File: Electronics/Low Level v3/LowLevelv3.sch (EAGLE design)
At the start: 66 parts, among them IC2 MCP4802, K1 ORWH-SH-105D1F,000, K3 ORWH-SH-105D1F,000, Q1 16MHz, T1 2N3904, T2 2N3904, U1 284512-4, U4 MCP2515, U5 MCP2551DIL08, X3 Motor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

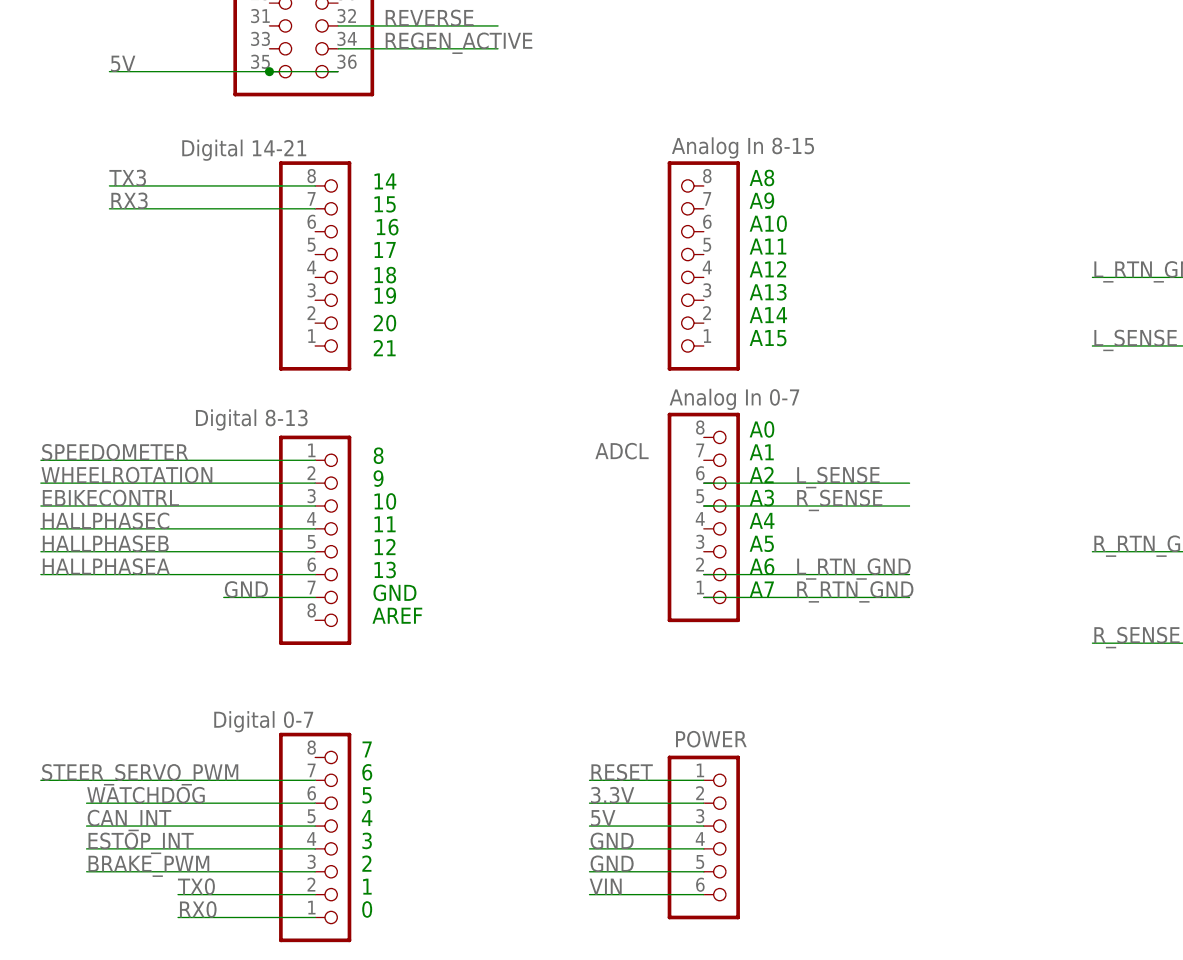
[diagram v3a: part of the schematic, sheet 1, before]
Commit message: corrected PCINT pin mapping
moved pretty much every interrupt pin to A8-A15, which had the secondary benefit of greatly reducing their trace length.
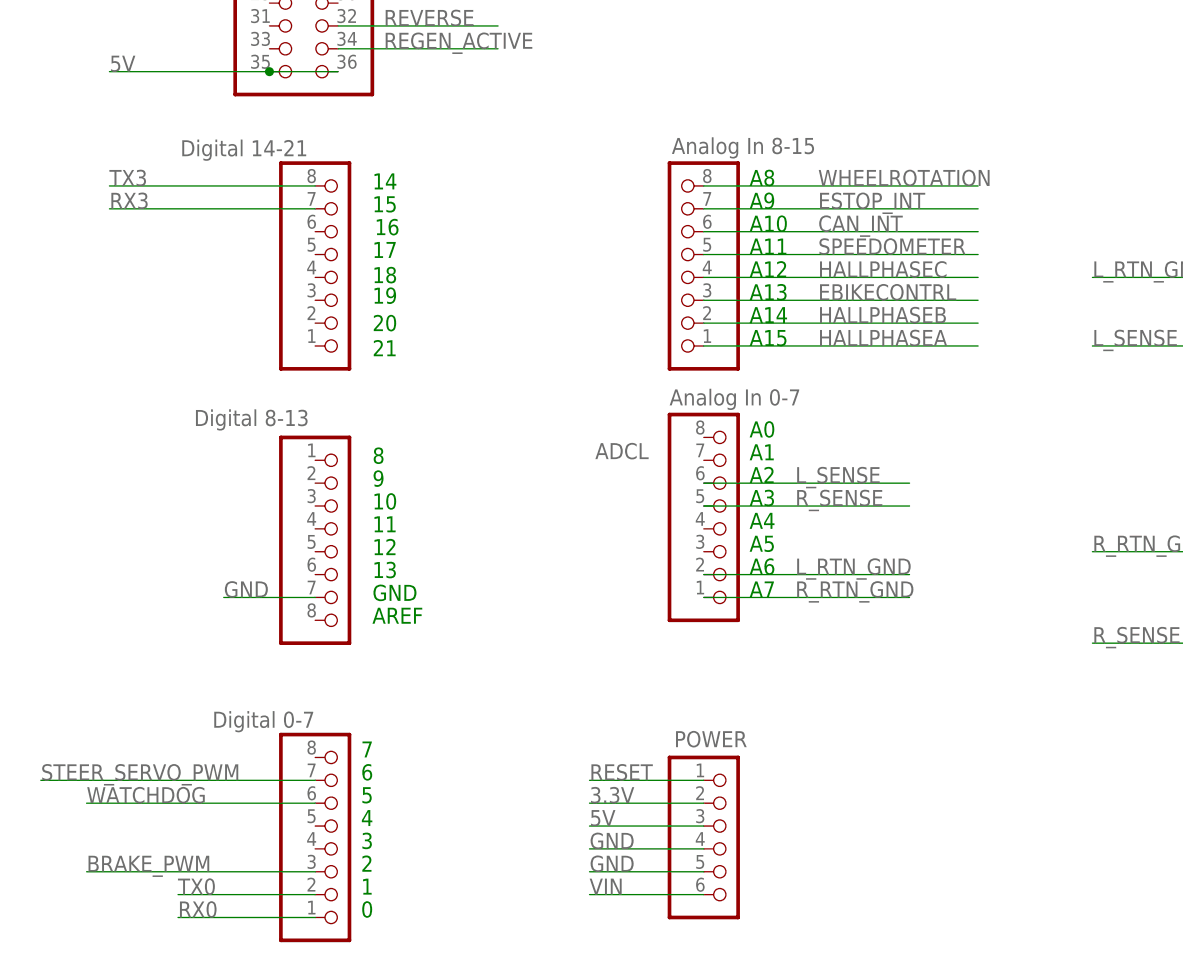
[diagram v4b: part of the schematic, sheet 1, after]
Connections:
- net CAN_INT: now also ADCH.6; no longer DIGITAL_0-7.5
- net EBIKECONTRL: now also ADCH.3; no longer DIGITAL_8-13.3
- net ESTOP_INT: now also ADCH.7; no longer DIGITAL_0-7.4
- net HALLPHASEA: now also ADCH.1; no longer DIGITAL_8-13.6
- net HALLPHASEB: now also ADCH.2; no longer DIGITAL_8-13.5
- net HALLPHASEC: now also ADCH.4; no longer DIGITAL_8-13.4
- net SPEEDOMETER: now also ADCH.5; no longer DIGITAL_8-13.1
- net WHEELROTATION: now also ADCH.8; no longer DIGITAL_8-13.2
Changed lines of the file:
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@@
 </segment>
 <segment>
-<label x="22.86" y="66.04" size="1.778" layer="95"/>
-<pinref part="DIGITAL_8-13" gate="A" pin="1"/>
-<wire x1="53.34" y1="66.04" x2="22.86" y2="66.04" width="0.1524" layer="91"/>
+<label x="109.22" y="88.9" size="1.778" layer="95"/>
+<pinref part="ADCH" gate="A" pin="5"/>
+<wire x1="127" y1="88.9" x2="96.52" y2="88.9" width="0.1524" layer="91"/>
 </segment>
 </net>
 <net name="HALLPHASEB" class="0">
 <segment>
-<label x="22.86" y="55.88" size="1.778" layer="95"/>
-<pinref part="DIGITAL_8-13" gate="A" pin="5"/>
-<wire x1="53.34" y1="55.88" x2="22.86" y2="55.88" width="0.1524" layer="91"/>
+<label x="109.22" y="81.28" size="1.778" layer="95"/>
+<pinref part="ADCH" gate="A" pin="2"/>
+<wire x1="96.52" y1="81.28" x2="127" y2="81.28" width="0.1524" layer="91"/>
 </segment>
 <segment>
@@
 <net name="WHEELROTATION" class="0">
 <segment>
-<label x="22.86" y="63.5" size="1.778" layer="95"/>
-<pinref part="DIGITAL_8-13" gate="A" pin="2"/>
-<wire x1="53.34" y1="63.5" x2="22.86" y2="63.5" width="0.1524" layer="91"/>
+<label x="109.22" y="96.52" size="1.778" layer="95"/>
+<pinref part="ADCH" gate="A" pin="8"/>
+<wire x1="96.52" y1="96.52" x2="127" y2="96.52" width="0.1524" layer="91"/>
 </segment>
 </net>
@@
 <net name="HALLPHASEA" class="0">
 <segment>
-<label x="22.86" y="53.34" size="1.778" layer="95"/>
-<pinref part="DIGITAL_8-13" gate="A" pin="6"/>
-<wire x1="53.34" y1="53.34" x2="22.86" y2="53.34" width="0.1524" layer="91"/>
+<label x="109.22" y="78.74" size="1.778" layer="95"/>
+<pinref part="ADCH" gate="A" pin="1"/>
+<wire x1="96.52" y1="78.74" x2="127" y2="78.74" width="0.1524" layer="91"/>
 </segment>
 <segment>
@@
 <net name="HALLPHASEC" class="0">
 <segment>
-<label x="22.86" y="58.42" size="1.778" layer="95"/>
-<pinref part="DIGITAL_8-13" gate="A" pin="4"/>
-<wire x1="53.34" y1="58.42" x2="22.86" y2="58.42" width="0.1524" layer="91"/>
+<label x="109.22" y="86.36" size="1.778" layer="95"/>
+<pinref part="ADCH" gate="A" pin="4"/>
+<wire x1="96.52" y1="86.36" x2="127" y2="86.36" width="0.1524" layer="91"/>
 </segment>
 <segment>
@@
 <net name="EBIKECONTRL" class="0">
 <segment>
-<label x="22.86" y="60.96" size="1.778" layer="95"/>
-<pinref part="DIGITAL_8-13" gate="A" pin="3"/>
-<wire x1="53.34" y1="60.96" x2="22.86" y2="60.96" width="0.1524" layer="91"/>
+<label x="109.22" y="83.82" size="1.778" layer="95"/>
+<pinref part="ADCH" gate="A" pin="3"/>
+<wire x1="96.52" y1="83.82" x2="127" y2="83.82" width="0.1524" layer="91"/>
 </segment>
 <segment>
@@
 <net name="CAN_INT" class="0">
 <segment>
-<label x="27.94" y="25.4" size="1.778" layer="95"/>
-<pinref part="DIGITAL_0-7" gate="A" pin="5"/>
-<wire x1="53.34" y1="25.4" x2="27.94" y2="25.4" width="0.1524" layer="91"/>
+<label x="109.22" y="91.44" size="1.778" layer="95"/>
+<pinref part="ADCH" gate="A" pin="6"/>
+<wire x1="96.52" y1="91.44" x2="127" y2="91.44" width="0.1524" layer="91"/>
 </segment>
 </net>
@@
 <net name="ESTOP_INT" class="0">
 <segment>
-<pinref part="DIGITAL_0-7" gate="A" pin="4"/>
-<wire x1="53.34" y1="22.86" x2="27.94" y2="22.86" width="0.1524" layer="91"/>
-<label x="27.94" y="22.86" size="1.778" layer="95"/>
-</segment>
-<segment>
+<label x="109.22" y="93.98" size="1.778" layer="95"/>
+<pinref part="ADCH" gate="A" pin="7"/>
+<wire x1="96.52" y1="93.98" x2="127" y2="93.98" width="0.1524" layer="91"/>
+</segment>
+<segment>

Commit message: board cleanup, via removal, silkscreen tidying
* Changing size of almost every 'tvalue' item
* slightly tweaked trace location to allow for greater ground plane coverage
* removed redundant ground vias
* began renaming devices for clarity
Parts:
- C3, C5, C8, C9: value 1 uF -> 1uF
- R3, R4, R8, R9: value 4.7 K -> 4.7K
- renumbered IC2 to IC3_4802, K1 to PB2_12/24, K3 to PB1_BRAKE_ON, U1 to X1, U4 to IC1_2515, U5 to IC2_2551

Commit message: lots of renaming and slight position changes
* renamed caps and resistors to make populating the board a little easier
* moved silk around to try and be a little more coherent
* slight copper adjustments to get more ground fill
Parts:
- C1, C2: value 0.1uF -> 1uF
- C11: value 33pF -> 0.1uF
- C13: value 560pF -> 0.1uF
- C4: value 1 uF -> 1uF
- C5: value 1uF -> 33pF
- C8: value 1uF -> 560pF
- C9: value 1uF -> 1 uF
- R1, R2: value 1K -> 4.7K
- R10: value 100 -> 120
- R11: value 4.7K -> 10k
- R12: value 120 -> 10k
- R13, R18: value 10k -> 1K
- R14: value 1K -> 20K
- R15: value 20K -> 10k
- R17: value 10k -> 4.7K
- R19: value 4.7K -> 1K
- R8: value 4.7K -> 100
- renumbered D5 to D4
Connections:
- net 5V: now also C11.1, C13.1, R14.1, R17.1; no longer C1.1, C2.1, R15.1, R19.1
- net BRAKE_ON: now also R18.1; no longer R6.1
- net CANH: now also R10.2; no longer R12.2
- net CANL: now also R10.1, R8.2; no longer R10.2, R12.1
- net ESTOP_INT: now also R15.1; no longer R17.1
- net GND: now also R12.2, R9.2; no longer R11.2, R18.2
- net L_RET: now also R2.2; no longer R9.2
- net L_RTN_GND: now also C2.1, R2.1; no longer C5.1, R9.1
- net L_SENSE: now also C1.1, R1.1; no longer C8.1, R4.1
- net L_STR: now also R1.2; no longer R4.2
- net N$1: now also R11.2, R12.1; no longer R13.2, R16.1
- net N$10: now also C8.1; no longer C13.1
- net N$12: now also R19.1; no longer R1.1
- net N$13: now also R19.2; no longer R1.2
- net N$14: now also R9.1; no longer R11.1
- net N$3: now also R6.1; no longer R2.1
- net N$4: now also R13.2; no longer R15.2
- net N$6: now also R6.2; no longer R2.2
- net N$7: now also R18.2; no longer R6.2
- net N$8: now also R15.2, R16.1; no longer R17.2, R18.1
- net N$9: now also R8.1; no longer R10.1
- net OSC2: now also C5.1; no longer C11.1
- net RESET: now also R11.1; no longer R13.1
- net RS: now also R13.1; no longer R14.1
- net R_RET: now also R4.2; no longer R8.2
- net R_RTN_GND: now also C4.1, R4.1; no longer C9.1, R8.1
- net WHEELROTATION: now also C9.1, R17.2; no longer C4.1, R19.2
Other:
- moved on the sheet: C11, C13, R11, R13, R14, R15, R16, R17, R4, R6

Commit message: Checkpoint for first PCB order
* few minor routing changes
* extended a 1x8 to a 1x10 because some Mega boards have two more pins on one header.
* added partial bill of materials
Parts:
- DIGITAL_8-13: device pinhead:PINHD-1X8 -> pinhead:PINHD-1X10
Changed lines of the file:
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@@
 <grid distance="0.1" unitdist="inch" unit="inch" style="lines" multiple="1" display="no" altdistance="0.01" altunitdist="inch" altunit="inch"/>
 <layers>
-<layer number="1" name="Top" color="4" fill="1" visible="yes" active="no"/>
-<layer number="2" name="Route2" color="1" fill="3" visible="yes" active="no"/>
-<layer number="3" name="Route3" color="4" fill="3" visible="yes" active="no"/>
-<layer number="4" name="Route4" color="1" fill="4" visible="yes" active="no"/>
-<layer number="5" name="Route5" color="4" fill="4" visible="yes" active="no"/>
-<layer number="6" name="Route6" color="1" fill="8" visible="yes" active="no"/>
-<layer number="7" name="Route7" color="4" fill="8" visible="yes" active="no"/>
-<layer number="8" name="Route8" color="1" fill="2" visible="yes" active="no"/>
-<layer number="9" name="Route9" color="4" fill="2" visible="yes" active="no"/>
-<layer number="10" name="Route10" color="1" fill="7" visible="yes" active="no"/>
-<layer number="11" name="Route11" color="4" fill="7" visible="yes" active="no"/>
-<layer number="12" name="Route12" color="1" fill="5" visible="yes" active="no"/>
-<layer number="13" name="Route13" color="4" fill="5" visible="yes" active="no"/>
-<layer number="14" name="Route14" color="1" fill="6" visible="yes" active="no"/>
-<layer number="15" name="Route15" color="4" fill="6" visible="yes" active="no"/>
-<layer number="16" name="Bottom" color="1" fill="1" visible="yes" active="no"/>
-<layer number="17" name="Pads" color="2" fill="1" visible="yes" active="no"/>
-<layer number="18" name="Vias" color="2" fill="1" visible="yes" active="no"/>
-<layer number="19" name="Unrouted" color="6" fill="1" visible="yes" active="no"/>
-<layer number="20" name="Dimension" color="15" fill="1" visible="yes" active="no"/>
-<layer number="21" name="tPlace" color="7" fill="1" visible="yes" active="no"/>
-<layer number="22" name="bPlace" color="7" fill="1" visible="yes" active="no"/>
-<layer number="23" name="tOrigins" color="15" fill="1" visible="yes" active="no"/>
-<layer number="24" name="bOrigins" color="15" fill="1" visible="yes" active="no"/>
-<layer number="25" name="tNames" color="7" fill="1" visible="yes" active="no"/>
-<layer number="26" name="bNames" color="7" fill="1" visible="yes" active="no"/>
-<layer number="27" name="tValues" color="7" fill="1" visible="yes" active="no"/>
-<layer number="28" name="bValues" color="7" fill="1" visible="yes" active="no"/>
+<layer number="1" name="Top" color="4" fill="1" visible="no" active="no"/>
+<layer number="2" name="Route2" color="1" fill="3" visible="no" active="no"/>
+<layer number="3" name="Route3" color="4" fill="3" visible="no" active="no"/>
+<layer number="4" name="Route4" color="1" fill="4" visible="no" active="no"/>
+<layer number="5" name="Route5" color="4" fill="4" visible="no" active="no"/>
+<layer number="6" name="Route6" color="1" fill="8" visible="no" active="no"/>
+<layer number="7" name="Route7" color="4" fill="8" visible="no" active="no"/>
+<layer number="8" name="Route8" color="1" fill="2" visible="no" active="no"/>
+<layer number="9" name="Route9" color="4" fill="2" visible="no" active="no"/>
+<layer number="10" name="Route10" color="1" fill="7" visible="no" active="no"/>
+<layer number="11" name="Route11" color="4" fill="7" visible="no" active="no"/>
+<layer number="12" name="Route12" color="1" fill="5" visible="no" active="no"/>
+<layer number="13" name="Route13" color="4" fill="5" visible="no" active="no"/>
+<layer number="14" name="Route14" color="1" fill="6" visible="no" active="no"/>
+<layer number="15" name="Route15" color="4" fill="6" visible="no" active="no"/>
+<layer number="16" name="Bottom" color="1" fill="1" visible="no" active="no"/>
+<layer number="17" name="Pads" color="2" fill="1" visible="no" active="no"/>
+<layer number="18" name="Vias" color="2" fill="1" visible="no" active="no"/>
+<layer number="19" name="Unrouted" color="6" fill="1" visible="no" active="no"/>
+<layer number="20" name="Dimension" color="15" fill="1" visible="no" active="no"/>
+<layer number="21" name="tPlace" color="7" fill="1" visible="no" active="no"/>
+<layer number="22" name="bPlace" color="7" fill="1" visible="no" active="no"/>
+<layer number="23" name="tOrigins" color="15" fill="1" visible="no" active="no"/>
+<layer number="24" name="bOrigins" color="15" fill="1" visible="no" active="no"/>
+<layer number="25" name="tNames" color="7" fill="1" visible="no" active="no"/>
+<layer number="26" name="bNames" color="7" fill="1" visible="no" active="no"/>
+<layer number="27" name="tValues" color="7" fill="1" visible="no" active="no"/>
+<layer number="28" name="bValues" color="7" fill="1" visible="no" active="no"/>
 <layer number="29" name="tStop" color="7" fill="3" visible="no" active="no"/>
 <layer number="30" name="bStop" color="7" fill="6" visible="no" active="no"/>
@@
 <layer number="35" name="tGlue" color="7" fill="4" visible="no" active="no"/>
 <layer number="36" name="bGlue" color="7" fill="5" visible="no" active="no"/>
-<layer number="37" name="tTest" color="7" fill="1" visible="yes" active="no"/>
-<layer number="38" name="bTest" color="7" fill="1" visible="yes" active="no"/>
+<layer number="37" name="tTest" color="7" fill="1" visible="no" active="no"/>
+<layer number="38" name="bTest" color="7" fill="1" visible="no" active="no"/>
 <layer number="39" name="tKeepout" color="4" fill="11" visible="no" active="no"/>
 <layer number="40" name="bKeepout" color="1" fill="11" visible="no" active="no"/>
@@
 <layer number="44" name="Drills" color="7" fill="1" visible="no" active="no"/>
 <layer number="45" name="Holes" color="7" fill="1" visible="no" active="no"/>
-<layer number="46" name="Milling" color="3" fill="1" visible="yes" active="no"/>
-<layer number="47" name="Measures" color="7" fill="1" visible="yes" active="no"/>
-<layer number="48" name="Document" color="7" fill="1" visible="yes" active="no"/>
-<layer number="49" name="Reference" color="7" fill="1" visible="yes" active="no"/>
-<layer number="50" name="dxf" color="12" fill="1" visible="yes" active="no"/>
-<layer number="51" name="tDocu" color="7" fill="1" visible="yes" active="no"/>
-<layer number="52" name="bDocu" color="7" fill="1" visible="yes" active="no"/>
-<layer number="53" name="tGND_GNDA" color="7" fill="1" visible="yes" active="no"/>
-<layer number="54" name="bGND_GNDA" color="7" fill="1" visible="yes" active="no"/>
-<layer number="56" name="wert" color="7" fill="1" visible="yes" active="no"/>
-<layer number="57" name="tCAD" color="7" fill="1" visible="yes" active="no"/>
-<layer number="59" name="tCarbon" color="7" fill="1" visible="yes" active="no"/>
-<layer number="60" name="bCarbon" color="7" fill="1" visible="yes" active="no"/>
+<layer number="46" name="Milling" color="3" fill="1" visible="no" active="no"/>
+<layer number="47" name="Measures" color="7" fill="1" visible="no" active="no"/>
+<layer number="48" name="Document" color="7" fill="1" visible="no" active="no"/>
+<layer number="49" name="Reference" color="7" fill="1" visible="no" active="no"/>
+<layer number="50" name="dxf" color="12" fill="1" visible="no" active="no"/>
+<layer number="51" name="tDocu" color="7" fill="1" visible="no" active="no"/>
+<layer number="52" name="bDocu" color="7" fill="1" visible="no" active="no"/>
+<layer number="53" name="tGND_GNDA" color="7" fill="1" visible="no" active="no"/>
+<layer number="54" name="bGND_GNDA" color="7" fill="1" visible="no" active="no"/>
+<layer number="56" name="wert" color="7" fill="1" visible="no" active="no"/>
+<layer number="57" name="tCAD" color="7" fill="1" visible="no" active="no"/>
+<layer number="59" name="tCarbon" color="7" fill="1" visible="no" active="no"/>
+<layer number="60" name="bCarbon" color="7" fill="1" visible="no" active="no"/>
 <layer number="88" name="SimResults" color="9" fill="1" visible="yes" active="yes"/>
 <layer number="89" name="SimProbes" color="9" fill="1" visible="yes" active="yes"/>
@@
 <part name="C1" library="resistor" library_urn="urn:adsk.eagle:library:348" deviceset="C-US" device="C1206" package3d_urn="urn:adsk.eagle:package:23618/2" value="1uF"/>
 <part name="C4" library="resistor" library_urn="urn:adsk.eagle:library:348" deviceset="C-US" device="C1206" package3d_urn="urn:adsk.eagle:package:23618/2" value="1uF"/>
-<part name="DIGITAL_8-13" library="pinhead" library_urn="urn:adsk.eagle:library:325" deviceset="PINHD-1X8" device="" package3d_urn="urn:adsk.eagle:package:22409/2" value="Digital 8-13"/>
+<part name="DIGITAL_8-13" library="pinhead" library_urn="urn:adsk.eagle:library:325" deviceset="PINHD-1X10" device="" package3d_urn="urn:adsk.eagle:package:22406/2" value="Digital 8-13"/>
 <part name="P+10" library="SparkFun-Aesthetics" library_urn="urn:adsk.eagle:library:507" deviceset="5V" device="">
 <attribute name="SPICEPREFIX" value="G"/>
